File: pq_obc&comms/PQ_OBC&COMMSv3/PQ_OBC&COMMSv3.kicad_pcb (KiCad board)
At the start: 4 copper layers, 40 x 40 mm, 66 parts, among them J1 Conn_01x10, J2 Conn_01x10, J3 Conn_01x10, J4 Conn_01x10, J6 U.FL-R-SMT-1_10_, U1 STM32L162RETx, U2 SX1262IMLTRT, U3 BD2232G-GTR, U4 BD2232G-GTR, U5 RFswitch, U7 BD2232G-GTR, X1 12MHz, X2 FA-128_32.0000MF20X-K5, X3 32.768KHz

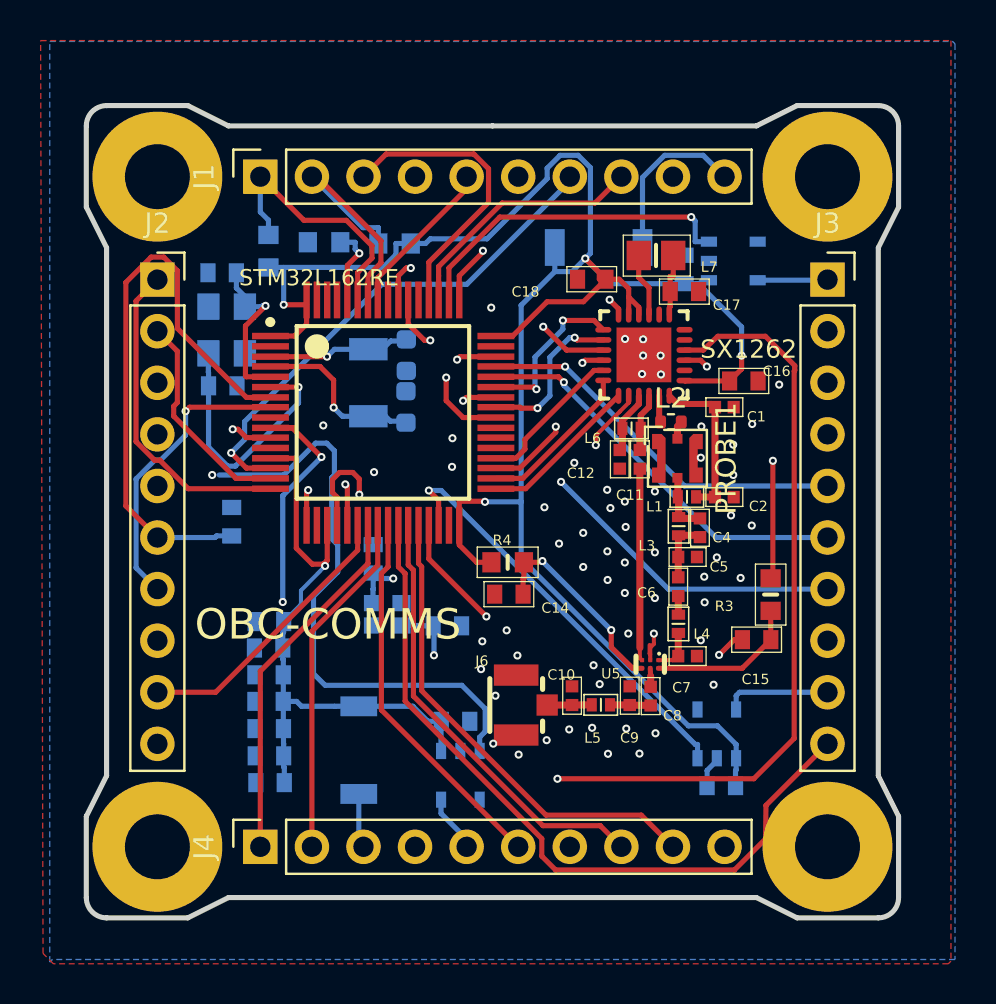
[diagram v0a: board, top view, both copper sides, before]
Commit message: gitkeep added to empty folders
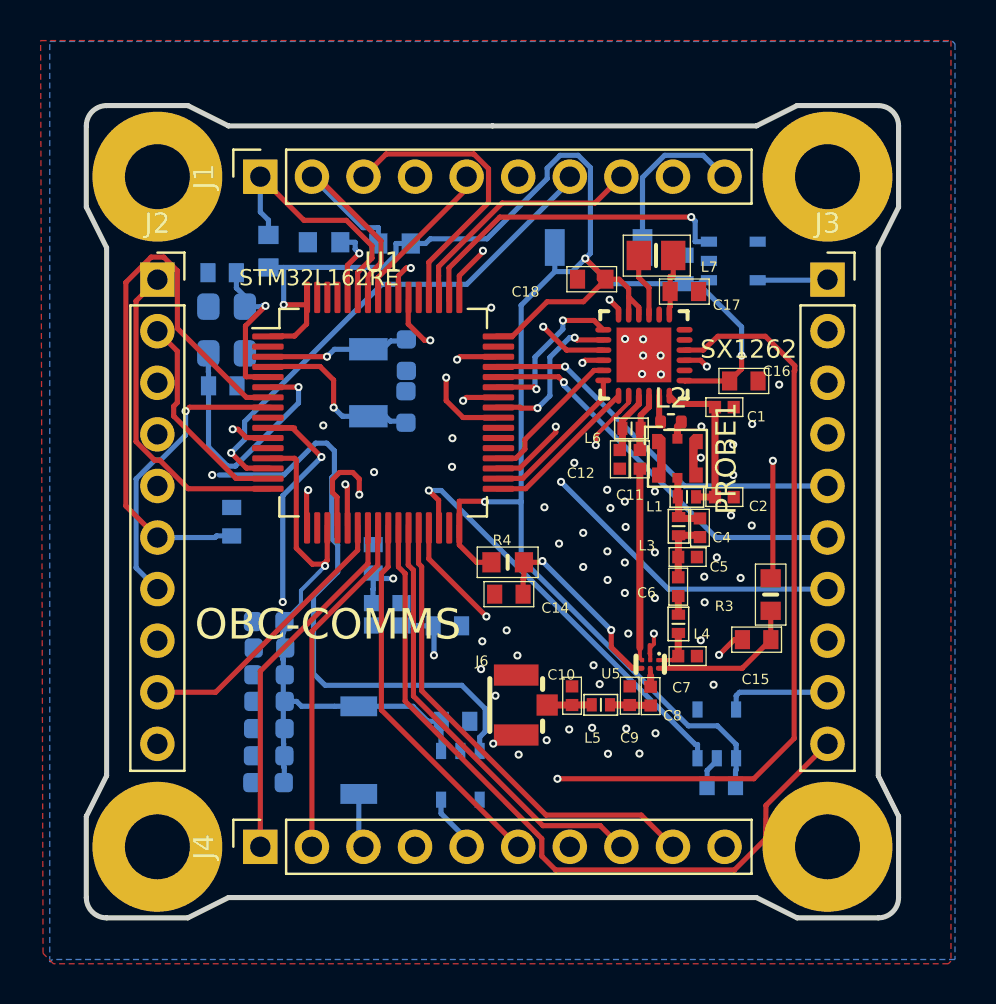
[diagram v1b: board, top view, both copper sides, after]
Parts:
- C31, C32, C33, C34, C35, C36, C37: footprint easyeda:CAPC1608X90N -> Capacitor_SMD:C_0603_1608Metric; moved to B.Cu
- U1: value STM32L162RETx -> STM32L476RGTx; footprint easyeda:STM-LQFP64 -> Package_QFP:LQFP-64_10x10mm_P0.5mm
- X1: footprint easyeda:ECS1201833JEMTR3 -> GGS_Miscellaneous:ECX-32; moved to B.Cu
- moved C37 0.10 mm to (88.1, 76.6), turned to 180 degrees
- turned C31 to 180 degrees
- turned C32 to 180 degrees
- turned C36 to 180 degrees
- turned C35 to 180 degrees
- turned C33 to 180 degrees
- turned C34 to 180 degrees
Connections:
- net ADC_PH1 renamed ADC_PH
- net ADC_PL2 renamed ADC_PL
- net BURNCOMMS_OBC renamed /PoL_BURN_EN
- net DAC_PL2 renamed DAC_PL
- net DIO1 renamed /DIO1
- net MISO renamed /MISO
- net MOSI renamed /MOSI
- net NRESET renamed /SX1262_NRST
- net NSS renamed /SX1262_NSS
- net Net-(R6-Pad1) renamed /Boot0
- net PALE renamed STM32_PB3
- net PCLK renamed STM32_PA2
- net PDATA renamed STM32_PD2
- net P/L_POWER_OBC renamed /PoL_P/L_EN
- net RST renamed EPS_RST
- net RX renamed UART_RX
- net SCK renamed /SCK
- net TX renamed UART_TX
- C16 pad 1: VCC -> VCC_UMBILICAL
- C18 pad 1: VCC -> VCC_UMBILICAL
- C31 pad 1: VCC -> VCC_UMBILICAL
- C32 pad 1: VCC -> VCC_UMBILICAL
- C33 pad 1: VCC -> VCC_UMBILICAL
- C34 pad 1: VCC -> VCC_UMBILICAL
- C35 pad 1: VCC -> VCC_UMBILICAL
- C36 pad 1: VCC -> VCC_UMBILICAL
- C37 pad 1: VCC -> VCC_UMBILICAL
- C43 pad 1: GND -> VCC_UMBILICAL
- C43 pad 2: VCC -> GND
- C44 pad 1: GND -> VCC_UMBILICAL
- C44 pad 2: VCC -> GND
- C45 pad 2: VCC -> VCC_UMBILICAL
- D1 pad 1: VCC -> 3V3
- D1 pad 2: Net-(D1-Pad2) -> VCC_UMBILICAL
- J1 pad 10: Net-(D1-Pad2) -> 3V3
- J1 pad 4: unconnected-(J1-Pad4) -> KILLSWITCH+
- J1 pad 6: unconnected-(J1-Pad6) -> BATT-
- J2 pad 7: CHGOFF -> CHRGOFF
- J3 pad 1: P/L2BURN_OBC -> STM32_PA15
- J3 pad 7: SEL -> HEATER_EN
- J3 pad 8: HEATER -> HEATER_PWR
- J4 pad 3: VCC_TEST1 -> VCC_UMBILICAL
- J4 pad 4: SEL_PH3 -> SEL_PH0
- R4 pad 1: VCC -> VCC_UMBILICAL
- R7 pad 1: VCC -> VCC_UMBILICAL
- R8 pad 1: VCC -> VCC_UMBILICAL
- U1 pad 1: VCC -> VCC_UMBILICAL
- U1 pad 13: VCC -> VCC_UMBILICAL
- U1 pad 17: SEL -> unconnected-(U1-Pad17)
- U1 pad 19: VCC -> VCC_UMBILICAL
- U1 pad 23: CHRG -> MPPT_Z
- U1 pad 28: MPPT_Z -> CHRG
- U1 pad 29: HEATER -> HEATER_EN
- U1 pad 32: VCC -> VCC_UMBILICAL
- U1 pad 41: BUSY -> /BUSY
- U1 pad 48: VCC -> VCC_UMBILICAL
- U1 pad 5: OSC_OUT -> OSC_IN
- U1 pad 50: P/L2BURN_OBC -> STM32_PA15
- U1 pad 6: OSC_IN -> OSC_OUT
- U1 pad 64: VCC -> VCC_UMBILICAL
- U2 pad 1: VCC -> VCC_UMBILICAL
- U2 pad 10: VCC -> VCC_UMBILICAL
- U2 pad 11: VCC -> VCC_UMBILICAL
- U2 pad 14: BUSY -> /SX1262_BUSY
- U3 pad 1: VCC -> VCC_UMBILICAL
- U4 pad 1: VCC -> VCC_UMBILICAL
- U7 pad 1: VCC -> VCC_UMBILICAL
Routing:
- net VCC_UMBILICAL: track 0.00 -> 149.6 mm, vias 0 -> 5
- net VCC: track 138.6 -> 0.00 mm, vias 5 -> 0
- net unconnected-(U1-Pad17): track 0.00 -> 33.5 mm, vias 0 -> 2
- net SEL: track 33.5 -> 0.00 mm, vias 2 -> 0
- net SEL_PH3: track 27.0 -> 0.00 mm, vias 2 -> 0
- net SEL_PH0: track 0.00 -> 27.0 mm, vias 0 -> 2
- net HEATER_EN: track 0.00 -> 23.0 mm, vias 0 -> 1
- net HEATER: track 23.0 -> 0.00 mm, vias 1 -> 0
- net CHRGOFF: track 0.00 -> 14.6 mm, vias 0 -> 1
- net CHGOFF: track 14.6 -> 0.00 mm, vias 1 -> 0
- net Net-(D1-Pad2): track 8.38 -> 0.00 mm
- net OSC32_IN: track 7.01 -> 15.0 mm, vias 1 -> 2
- net OSC_OUT: track 20.9 -> 12.9 mm, vias 2 -> 1
- net BUSY: track 7.90 -> 0.00 mm, vias 2 -> 0
- net /SX1262_BUSY: track 0.00 -> 7.90 mm, vias 0 -> 2
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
